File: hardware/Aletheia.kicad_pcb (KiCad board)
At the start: 12 copper layers, 94 x 127 mm, 85 parts, among them J101 Conn_01x04, J201 4090 USB-C, J202 9V battery, SW101 SW_DIP_x08, SW102 SW_DIP_x08, SW104 SW_DIP_x04, SW105 G19AP, SW301 Q/1/STOP, SW302 W/2/CH0, SW303 E/3/CH1, SW304 R/4/CH2, SW305 T/5/CH3, SW306 Y/6/_, SW307 U/7/-, SW308 I/8/+, SW309 O/9/=, SW310 P/0, SW311 A/!/`, SW312 S/"/CH4, SW313 D/$/CH5, SW314 F/%/CH6, SW315 G/^/CH7, SW316 H/&/{, SW317 J/*/}, SW318 K/(/[, SW319 L/)/], SW320 BKSP/DEL, SW321 SHIFT, SW322 Z/\/|, SW323 X/;/:, SW324 C/'/@, SW325 V/#/~, SW326 B/,/<, SW327 N/./>, SW328 M///?, SW329 SYM, SW330 SPC/ENT, U101 W65C02S6TPG-14, U102 AS6C1008-55PCN, U103 W65C22N6TPG-14, U104 74LS04, U105 74LS08, U106 74LS21, U201 LP2954AIT/NOPB, U301 MCP23S17_SP, U302 NHD-0420DZ-NSW-BBW, Y101 ECS-100AX-010

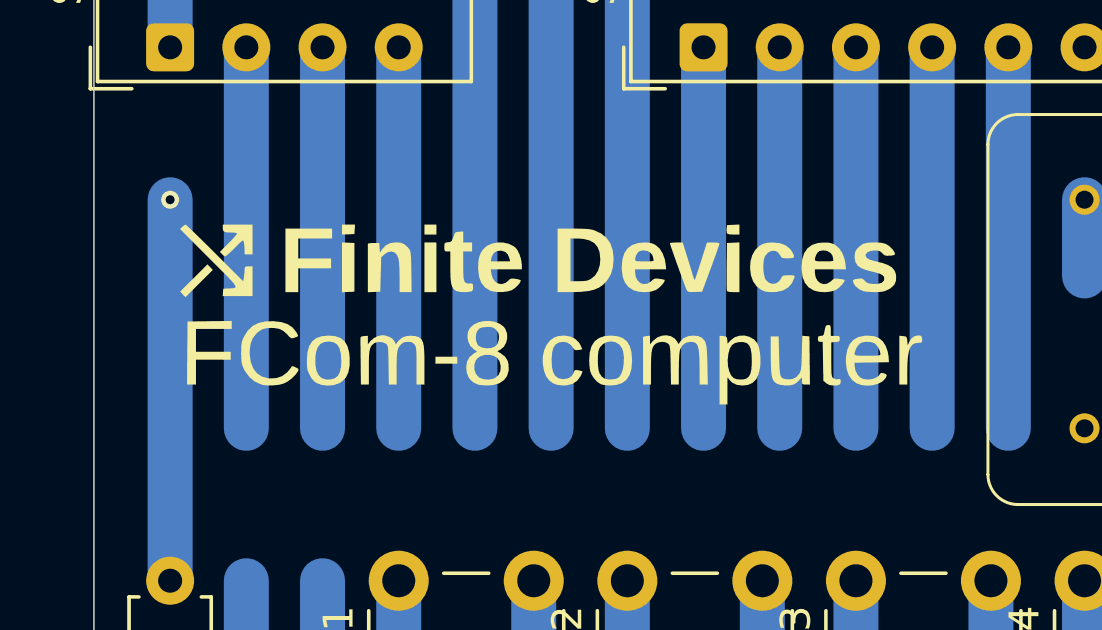
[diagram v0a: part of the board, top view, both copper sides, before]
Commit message: Update design files to reflect new name
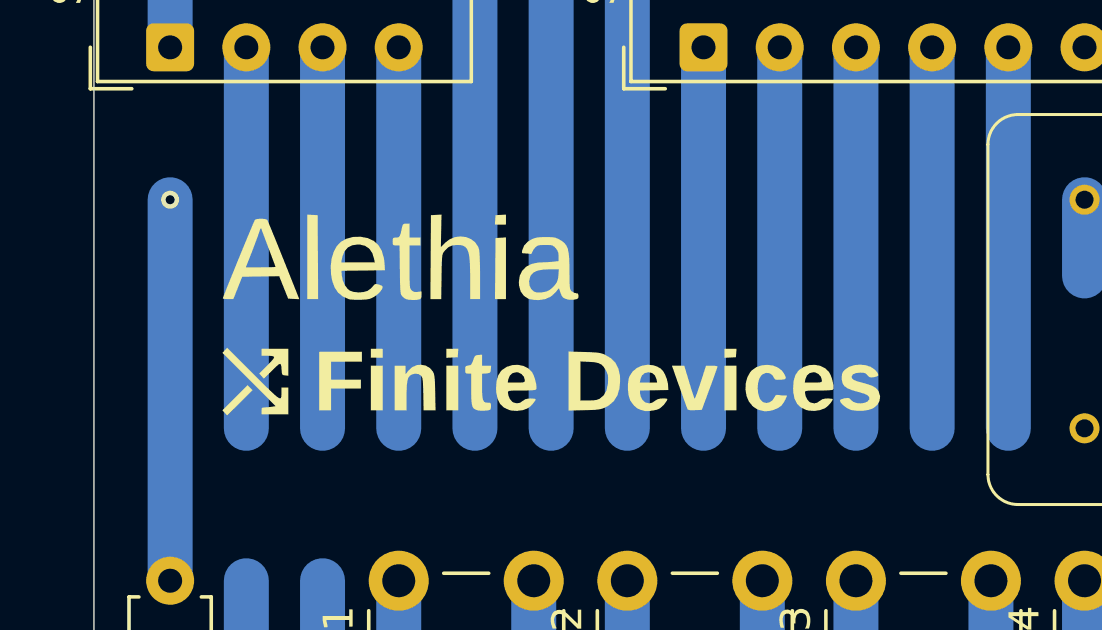
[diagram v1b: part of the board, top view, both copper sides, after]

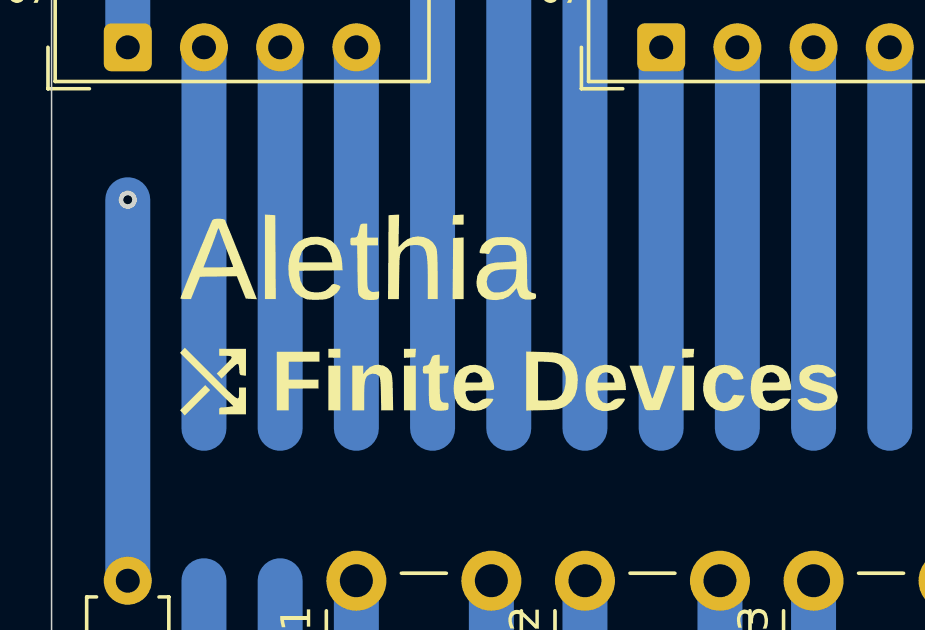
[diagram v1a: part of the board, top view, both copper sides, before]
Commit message: Fix typo in branding files
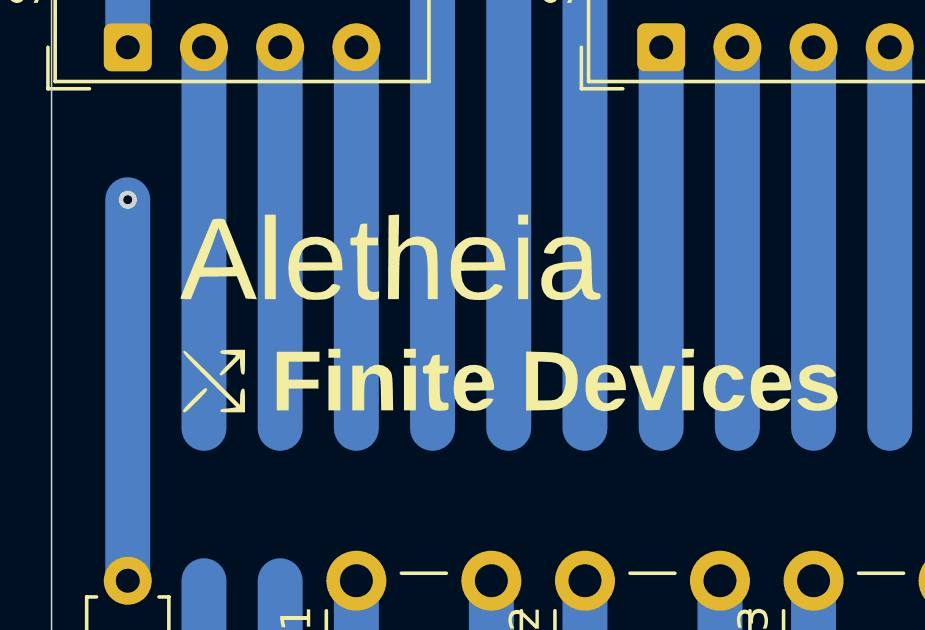
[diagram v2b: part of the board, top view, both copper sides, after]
